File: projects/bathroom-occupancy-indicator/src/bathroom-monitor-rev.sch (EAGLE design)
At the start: 18 parts, among them IC1 7805T, J1 12V, T1 2N2222, U1 ATTINY85-20PU, U2 ATTINY85-20PU

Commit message: pictures cleanup + instructions in progress
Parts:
- D1: value (none) -> 1N4001
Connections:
- net N$6: now also D1.C; no longer D1.A
- net VCC: now also D1.A; no longer D1.C
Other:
- moved on the sheet: D1
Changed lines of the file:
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@@
 <part name="GND8" library="SparkFun-Aesthetics" deviceset="GND" device=""/>
 <part name="J1" library="con-jack" deviceset="JACK-PLUG" device="1" value="12V"/>
-<part name="D1" library="SparkFun-DiscreteSemi" deviceset="DIODE" device="KIT2"/>
+<part name="D1" library="SparkFun-DiscreteSemi" deviceset="DIODE" device="KIT2" value="1N4001"/>
 <part name="T1" library="adafruit" deviceset="2N2222" device=""/>
 </parts>
@@
 <instance part="GND8" gate="1" x="149.86" y="10.16"/>
 <instance part="J1" gate="G$1" x="22.86" y="109.22"/>
-<instance part="D1" gate="G$1" x="104.14" y="17.78" smashed="yes">
-<attribute name="NAME" x="102.87" y="20.2946" size="1.778" layer="95"/>
-<attribute name="VALUE" x="106.68" y="15.4686" size="1.778" layer="96"/>
+<instance part="D1" gate="G$1" x="104.14" y="17.78" smashed="yes" rot="R180">
+<attribute name="NAME" x="105.41" y="15.2654" size="1.778" layer="95" rot="R180"/>
+<attribute name="VALUE" x="110.236" y="21.6154" size="1.778" layer="96" rot="R180"/>
 </instance>
 <instance part="T1" gate="G$1" x="198.374" y="100.584" rot="R270"/>
@@
 </segment>
 <segment>
+<pinref part="D1" gate="G$1" pin="A"/>
 <pinref part="SUPPLY3" gate="G$1" pin="VCC"/>
-<pinref part="D1" gate="G$1" pin="C"/>
-<wire x1="109.22" y1="17.78" x2="106.68" y2="17.78" width="0.1524" layer="91"/>
+<wire x1="106.68" y1="17.78" x2="109.22" y2="17.78" width="0.1524" layer="91"/>
 </segment>
 </net>
@@
 </segment>
 </net>
-<net name="N$6" class="0">
-<segment>
-<pinref part="D1" gate="G$1" pin="A"/>
-<pinref part="L1" gate="G$1" pin="VDD"/>
-<wire x1="101.6" y1="17.78" x2="96.52" y2="17.78" width="0.1524" layer="91"/>
-</segment>
-</net>
 <net name="N$8" class="0">
 <segment>
@@
 </segment>
 </net>
+<net name="N$6" class="0">
+<segment>
+<pinref part="D1" gate="G$1" pin="C"/>
+<pinref part="L1" gate="G$1" pin="VDD"/>
+<wire x1="101.6" y1="17.78" x2="96.52" y2="17.78" width="0.1524" layer="91"/>
+</segment>
+</net>

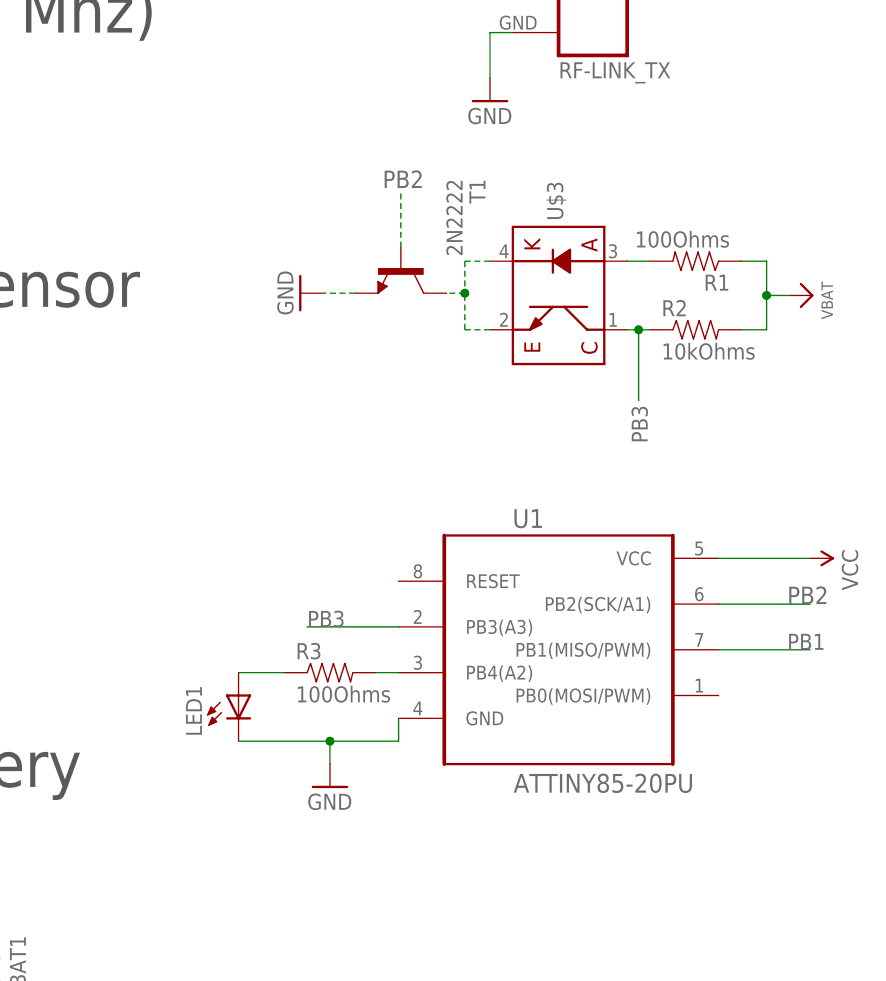
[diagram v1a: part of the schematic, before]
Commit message: Correction on circuit schematics
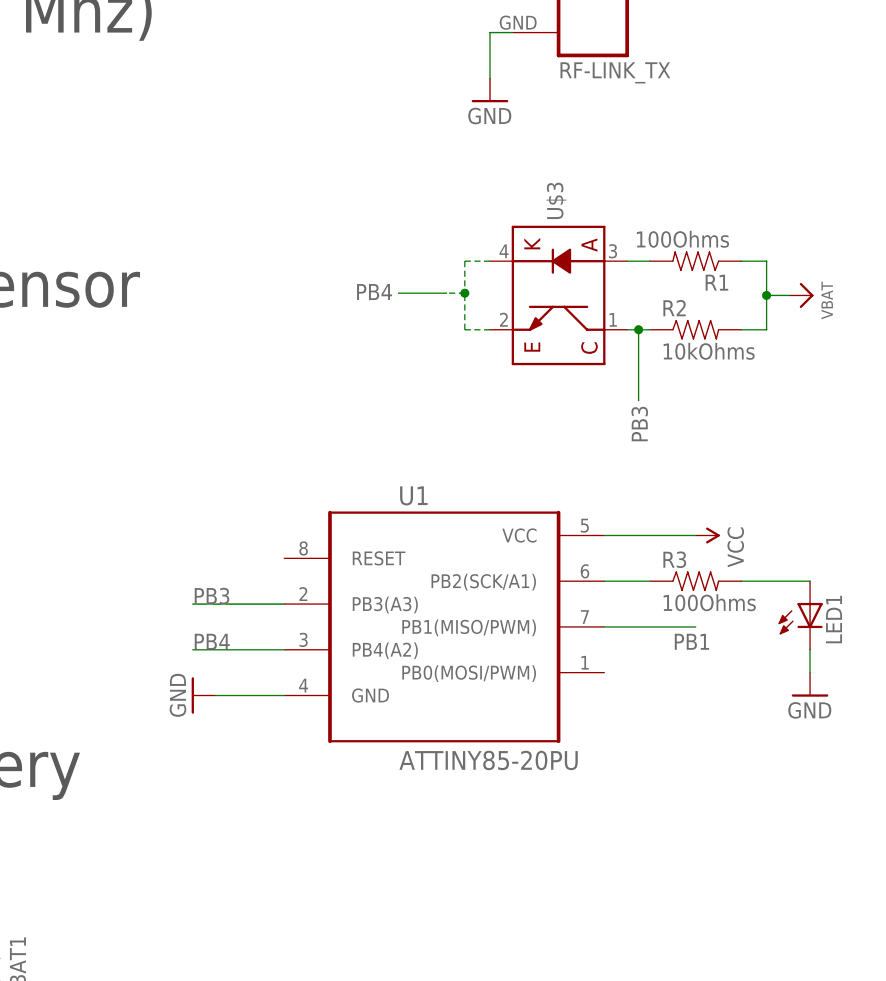
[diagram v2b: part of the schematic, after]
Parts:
- removed T1: 2N2222, adafruit:2N2222
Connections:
- removed net N$8: T1.C, U$3.C, U$3.K
- removed net PB2: T1.B, U1.PB2(SCK/A1)
- new net PB4: U$3.C, U$3.K, U1.PB4(A2)
- net GND: no longer T1.E
- net N$5: now also R3.1, U1.PB2(SCK/A1); no longer R3.2, U1.PB4(A2)
- net N$7: now also R3.2; no longer R3.1
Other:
- moved on the sheet: LED1, R3, U1
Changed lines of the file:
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@@
 <part name="L1" library="adafruit" deviceset="WS2812B" device=""/>
 <part name="FRAME1" library="microbuilder" deviceset="FRAME_A4" device=""/>
-<part name="LED1" library="adafruit" deviceset="LED" device="3MM"/>
-<part name="R3" library="SparkFun-Resistors" deviceset="RESISTOR" device="PTH-1/2W" value="100Ohms"/>
 <part name="SUPPLY1" library="SparkFun-Aesthetics" deviceset="VCC" device=""/>
-<part name="GND1" library="SparkFun-Aesthetics" deviceset="GND" device=""/>
 <part name="GND2" library="SparkFun-Aesthetics" deviceset="GND" device=""/>
 <part name="SUPPLY2" library="SparkFun-Aesthetics" deviceset="VCC" device=""/>
@@
 <part name="GND6" library="SparkFun-Aesthetics" deviceset="GND" device=""/>
 <part name="SUPPLY4" library="SparkFun-Aesthetics" deviceset="VCC" device=""/>
-<part name="GND7" library="SparkFun-Aesthetics" deviceset="GND" device=""/>
 <part name="U$7" library="microbuilder" deviceset="VBAT" device=""/>
 <part name="U$8" library="microbuilder" deviceset="VBAT" device=""/>
@@
 <part name="J1" library="con-jack" deviceset="JACK-PLUG" device="1" value="12V"/>
 <part name="D1" library="SparkFun-DiscreteSemi" deviceset="DIODE" device="KIT2" value="1N4001"/>
-<part name="T1" library="adafruit" deviceset="2N2222" device=""/>
+<part name="R3" library="SparkFun-Resistors" deviceset="RESISTOR" device="PTH-1/2W" value="100Ohms"/>
+<part name="LED1" library="adafruit" deviceset="LED" device="3MM"/>
+<part name="GND7" library="SparkFun-Aesthetics" deviceset="GND" device=""/>
+<part name="GND1" library="SparkFun-Aesthetics" deviceset="GND" device=""/>
 </parts>
 <sheets>
@@
 </plain>
 <instances>
-<instance part="U1" gate="A" x="215.9" y="58.42"/>
+<instance part="U1" gate="A" x="203.2" y="60.96"/>
 <instance part="U2" gate="A" x="48.26" y="149.86"/>
 <instance part="U$1" gate="G$1" x="40.64" y="66.04"/>
@@
 <instance part="L1" gate="G$1" x="91.44" y="17.78" rot="R270"/>
 <instance part="FRAME1" gate="G$1" x="0" y="0"/>
-<instance part="LED1" gate="G$1" x="180.34" y="53.34" smashed="yes">
-<attribute name="NAME" x="176.276" y="48.768" size="1.778" layer="95" rot="R90"/>
-<attribute name="VALUE" x="186.055" y="48.768" size="1.778" layer="96" rot="R90"/>
-</instance>
-<instance part="R3" gate="G$1" x="190.5" y="55.88"/>
-<instance part="SUPPLY1" gate="G$1" x="243.84" y="68.58" rot="R270"/>
-<instance part="GND1" gate="1" x="190.5" y="43.18"/>
+<instance part="SUPPLY1" gate="G$1" x="231.14" y="71.12" rot="R270"/>
 <instance part="GND2" gate="1" x="48.26" y="99.06"/>
 <instance part="SUPPLY2" gate="G$1" x="68.58" y="111.76" rot="R270"/>
@@
 <instance part="GND6" gate="1" x="25.4" y="53.34"/>
 <instance part="SUPPLY4" gate="G$1" x="25.4" y="81.28"/>
-<instance part="GND7" gate="1" x="187.198" y="98.044" rot="R270"/>
 <instance part="U$7" gate="G$1" x="244.094" y="97.79" rot="R270"/>
 <instance part="U$8" gate="G$1" x="149.86" y="35.56"/>
@@
 <attribute name="VALUE" x="110.236" y="21.6154" size="1.778" layer="96" rot="R180"/>
 </instance>
-<instance part="T1" gate="G$1" x="198.374" y="100.584" rot="R270"/>
+<instance part="R3" gate="G$1" x="231.14" y="66.04"/>
+<instance part="LED1" gate="G$1" x="243.84" y="63.5" smashed="yes">
+<attribute name="NAME" x="247.396" y="58.928" size="1.778" layer="95" rot="R90"/>
+<attribute name="VALUE" x="249.555" y="58.928" size="1.778" layer="96" rot="R90"/>
+</instance>
+<instance part="GND7" gate="1" x="175.26" y="53.34" rot="R270"/>
+<instance part="GND1" gate="1" x="243.84" y="53.34"/>
 </instances>
 <busses>
@@
 </segment>
 <segment>
-<pinref part="T1" gate="G$1" pin="E"/>
-<pinref part="GND7" gate="1" pin="GND"/>
-<wire x1="193.294" y1="98.044" x2="189.738" y2="98.044" width="0.1524" layer="91" style="longdash"/>
-</segment>
-<segment>
-<pinref part="LED1" gate="G$1" pin="C"/>
-<wire x1="180.34" y1="48.26" x2="190.5" y2="48.26" width="0.1524" layer="91"/>
-<pinref part="GND1" gate="1" pin="GND"/>
-<wire x1="190.5" y1="48.26" x2="190.5" y2="45.72" width="0.1524" layer="91"/>
-<pinref part="U1" gate="A" pin="GND"/>
-<wire x1="198.12" y1="50.8" x2="198.12" y2="48.26" width="0.1524" layer="91"/>
-<wire x1="198.12" y1="48.26" x2="190.5" y2="48.26" width="0.1524" layer="91"/>
-<junction x="190.5" y="48.26"/>
-</segment>
-<segment>
 <pinref part="GND4" gate="1" pin="GND"/>
 <pinref part="U2" gate="A" pin="GND"/>
 <wire x1="20.32" y1="142.24" x2="30.48" y2="142.24" width="0.1524" layer="91"/>
 </segment>
+<segment>
+<pinref part="U1" gate="A" pin="GND"/>
+<wire x1="185.42" y1="53.34" x2="177.8" y2="53.34" width="0.1524" layer="91"/>
+<pinref part="GND7" gate="1" pin="GND"/>
+</segment>
+<segment>
+<pinref part="LED1" gate="G$1" pin="C"/>
+<pinref part="GND1" gate="1" pin="GND"/>
+<wire x1="243.84" y1="58.42" x2="243.84" y2="55.88" width="0.1524" layer="91"/>
+</segment>
 </net>
 <net name="PB1" class="0">
 <segment>
 <pinref part="U1" gate="A" pin="PB1(MISO/PWM)"/>
-<wire x1="233.68" y1="58.42" x2="243.84" y2="58.42" width="0.1524" layer="91"/>
-<label x="241.3" y="58.42" size="1.778" layer="95"/>
+<wire x1="220.98" y1="60.96" x2="231.14" y2="60.96" width="0.1524" layer="91"/>
+<label x="228.6" y="58.42" size="1.778" layer="95"/>
 </segment>
 <segment>
@@
 <segment>
 <pinref part="U1" gate="A" pin="VCC"/>
-<wire x1="233.68" y1="68.58" x2="243.84" y2="68.58" width="0.1524" layer="91"/>
+<wire x1="220.98" y1="71.12" x2="231.14" y2="71.12" width="0.1524" layer="91"/>
 <pinref part="SUPPLY1" gate="G$1" pin="VCC"/>
 </segment>
@@
 <segment>
 <pinref part="U1" gate="A" pin="PB3(A3)"/>
-<wire x1="198.12" y1="60.96" x2="187.96" y2="60.96" width="0.1524" layer="91"/>
-<label x="187.96" y="60.96" size="1.778" layer="95"/>
+<wire x1="185.42" y1="63.5" x2="175.26" y2="63.5" width="0.1524" layer="91"/>
+<label x="175.26" y="63.5" size="1.778" layer="95"/>
 </segment>
 <segment>
@@
 </segment>
 </net>
-<net name="N$8" class="0">
+<net name="N$6" class="0">
+<segment>
+<pinref part="D1" gate="G$1" pin="C"/>
+<pinref part="L1" gate="G$1" pin="VDD"/>
+<wire x1="101.6" y1="17.78" x2="96.52" y2="17.78" width="0.1524" layer="91"/>
+</segment>
+</net>
+<net name="PB4" class="0">
+<segment>
+<pinref part="U1" gate="A" pin="PB4(A2)"/>
+<wire x1="185.42" y1="58.42" x2="175.26" y2="58.42" width="0.1524" layer="91"/>
+<label x="175.26" y="58.42" size="1.778" layer="95"/>
+</segment>
 <segment>
 <pinref part="U$3" gate="G$1" pin="K"/>
 <wire x1="208.28" y1="101.6" x2="205.486" y2="101.6" width="0.1524" layer="91" style="longdash"/>
 <wire x1="205.486" y1="101.6" x2="205.486" y2="98.044" width="0.1524" layer="91" style="longdash"/>
-<pinref part="T1" gate="G$1" pin="C"/>
 <wire x1="205.486" y1="98.044" x2="203.454" y2="98.044" width="0.1524" layer="91" style="longdash"/>
 <pinref part="U$3" gate="G$1" pin="C"/>
@@
 <wire x1="205.486" y1="93.98" x2="205.486" y2="98.044" width="0.1524" layer="91" style="longdash"/>
 <junction x="205.486" y="98.044"/>
-</segment>
-</net>
-<net name="PB2" class="0">
+<wire x1="203.454" y1="98.044" x2="198.12" y2="98.044" width="0.1524" layer="91"/>
+<label x="193.294" y="97.282" size="1.778" layer="95"/>
+</segment>
+</net>
+<net name="N$5" class="0">
 <segment>
 <pinref part="U1" gate="A" pin="PB2(SCK/A1)"/>
-<wire x1="233.68" y1="63.5" x2="243.84" y2="63.5" width="0.1524" layer="91"/>
-<label x="241.3" y="63.5" size="1.9304" layer="95"/>
-</segment>
-<segment>
-<pinref part="T1" gate="G$1" pin="B"/>
-<wire x1="198.374" y1="103.124" x2="198.374" y2="109.22" width="0.1524" layer="91" style="longdash"/>
-<label x="196.342" y="109.728" size="1.9304" layer="95"/>
-</segment>
-</net>
-<net name="N$5" class="0">
-<segment>
-<pinref part="U1" gate="A" pin="PB4(A2)"/>
+<pinref part="R3" gate="G$1" pin="1"/>
+<wire x1="220.98" y1="66.04" x2="226.06" y2="66.04" width="0.1524" layer="91"/>
+</segment>
+</net>
+<net name="N$7" class="0">
+<segment>
 <pinref part="R3" gate="G$1" pin="2"/>
-<wire x1="198.12" y1="55.88" x2="195.58" y2="55.88" width="0.1524" layer="91"/>
-</segment>
-</net>
-<net name="N$7" class="0">
-<segment>
-<pinref part="R3" gate="G$1" pin="1"/>
 <pinref part="LED1" gate="G$1" pin="A"/>
-<wire x1="185.42" y1="55.88" x2="180.34" y2="55.88" width="0.1524" layer="91"/>
-</segment>
-</net>
-<net name="N$6" class="0">
-<segment>
-<pinref part="D1" gate="G$1" pin="C"/>
-<pinref part="L1" gate="G$1" pin="VDD"/>
-<wire x1="101.6" y1="17.78" x2="96.52" y2="17.78" width="0.1524" layer="91"/>
-</segment>
-</net>
+<wire x1="236.22" y1="66.04" x2="243.84" y2="66.04" width="0.1524" layer="91"/>
+</segment>
+</net>
